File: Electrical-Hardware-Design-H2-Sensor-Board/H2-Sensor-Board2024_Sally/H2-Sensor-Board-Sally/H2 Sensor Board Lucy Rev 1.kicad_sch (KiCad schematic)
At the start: 55 parts, among them IC1 ESDALC6V1W5, J1 GPIO, J4 USB_B_Micro, J5 Conn_02x05_Top_Bottom, J8 OLED, Q2 NMOS IRLML2502TRPBF, SW1 SW_SPDT, SW2 RESET, U1 STM32L432KCU6, U10 8MHz, U10 MCP2542FD-E/SN, U7 FT234XD-R

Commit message: system update
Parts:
- added C1, C29, C30: 100n, Capacitor_SMD:C_0402_1005Metric, symbol Device:C
- added C10 (x2): 22u, Capacitor_SMD:CP_Elec_6.3x5.9, symbol Device:C_Polarized
- added C10: 100u, Capacitor_SMD:CP_Elec_6.3x5.9, symbol Device:C_Polarized
- added C15, C18: 100n, Capacitor_SMD:C_0603_1608Metric, symbol Device:C
- added C16, C17: 22u, Capacitor_SMD:C_1210_3225Metric, symbol Device:C
- added C2: 100n, Capacitor_SMD:C_0402_1005Metric, symbol Device:C_Small
- added C2: 100n, Capacitor_SMD:C_0603_1608Metric, symbol Device:C_Small
- added C21, C23: 10u, Capacitor_SMD:C_0805_2012Metric, symbol Device:C
- added C22, C24: 22u, Capacitor_SMD:C_0805_2012Metric, symbol Device:C
- added C25: 100n, Capacitor_SMD:C_0805_2012Metric, symbol Device:C
- added C28: 10u, Capacitor_SMD:C_1210_3225Metric, symbol Device:C
- added C32: 2n2, Capacitor_SMD:C_0402_1005Metric, symbol Device:C
- added C36, C37: 0u1, Capacitor_SMD:C_0603_1608Metric, symbol Device:C
- added C38: 4u7, Capacitor_SMD:C_0603_1608Metric, symbol Device:C
- added C39: 10n, Capacitor_SMD:C_0603_1608Metric, symbol Device:C
- added C40: 1u, Capacitor_SMD:C_0603_1608Metric, symbol Device:C
- added D1: GREEN, LED_SMD:LED_0805_2012Metric, symbol Device:LED
- added D11: BAT54C, Package_TO_SOT_SMD:SOT-23, symbol Diode:BAT54C
- added D14, D2, D3, D4: BLUE, LED_SMD:LED_0805_2012Metric, symbol Device:LED
- added D5: MMSZ5226B-7-F, Diode_SMD:D_SOD-123, symbol Device:D_Zener
- added D9: D_Schottky, Diode_SMD:D_0805_2012Metric, symbol Device:D_Schottky
- added F1: 500mA, Fuse:Fuse_0805_2012Metric, symbol Device:Polyfuse
- added FB2: 120R, Inductor_SMD:L_0603_1608Metric, symbol Device:FerriteBead_Small
- added J2: Conn_02x03_Top_Bottom, SYM&FOOT:Molex_Micro-Fit_3.0_43045-0621_2x03-1MP_P3.00mm_Horizontal, symbol Connector_Generic:Conn_02x03_Top_Bottom
- added JP1: Slave Address LSB 1, Jumper:SolderJumper-2_P1.3mm_Bridged_RoundedPad1.0x1.5mm, symbol Jumper:Jumper_2_Bridged
- added JP2: Slave Address LSB 0, Jumper:SolderJumper-2_P1.3mm_Open_RoundedPad1.0x1.5mm, symbol Jumper:Jumper_2_Open
- added JP3: MAX CURRENT, Jumper:SolderJumper-2_P1.3mm_Bridged_RoundedPad1.0x1.5mm, symbol Jumper:Jumper_2_Bridged
- added L1: 3u8, Inductor_SMD:L_12x12mm_H8mm, symbol Device:L
- added NT1: NetTie_2, NetTie:NetTie-2_SMD_Pad2.0mm, symbol Device:NetTie_2
- added Q1: NMOS, Package_TO_SOT_SMD:SOT-23, symbol Simulation_SPICE:NMOS
- added R1: 4k7, Resistor_SMD:R_0603_1608Metric, symbol Device:R_US
- added R10, R19: 560R, Resistor_SMD:R_0805_2012Metric, symbol Device:R
- added R11: 220R, Resistor_SMD:R_0805_2012Metric, symbol Device:R
- added R12, R7: 2k, Resistor_SMD:R_0805_2012Metric, symbol Device:R
- added R2: 620R, Resistor_SMD:R_0603_1608Metric, symbol Device:R
- added R20: R, Resistor_THT:R_Axial_DIN0204_L3.6mm_D1.6mm_P7.62mm_Horizontal, symbol Device:R
- added R21, R22, R3: 4k7, Resistor_SMD:R_0603_1608Metric, symbol Device:R
- added R27: 30k, Resistor_SMD:R_0603_1608Metric, symbol Device:R
- added R28: 47k, Resistor_SMD:R_0603_1608Metric, symbol Device:R
- added R30: 10k, Resistor_SMD:R_0805_2012Metric, symbol Device:R_US
- added R4, R8: 47k, Resistor_SMD:R_0805_2012Metric, symbol Device:R
- added R5: 23k7, Resistor_SMD:R_0805_2012Metric, symbol Device:R
- added R6: 511k, Resistor_SMD:R_0805_2012Metric, symbol Device:R
- added R9: 6k2, Resistor_SMD:R_0805_2012Metric, symbol Device:R
- added SW2: TARE, Button_Switch_THT:SW_PUSH_6mm_H5mm, symbol Switch:SW_Push
- added SW4: SW_SPDT, Button_Switch_SMD:SW_SPDT_PCM12, symbol Switch:SW_SPDT
- added TP3: MCO, TestPoint:TestPoint_Pad_D1.0mm, symbol Connector:TestPoint
- added U10: ~, SYM&FOOT:H2_Sensor_Daughter_Board_Rev_1, symbol H2_Parts:H2_Simon_Sensor_Breakout
- added U11: AD8603, Package_TO_SOT_SMD:TSOT-23-5, symbol Amplifier_Operational:AD8603
- added U12: STM32G474RET6, Package_QFP:LQFP-64_10x10mm_P0.5mm, symbol MCU_ST_STM32G4:STM32G474RETx
- added U3: AZ1117IH-5.0, Package_TO_SOT_SMD:SOT-223-3_TabPin2, symbol H2_Parts:AZ111IH-5.0
- added U4: TPS2596, Package_SO:TI_SO-PowerPAD-8, symbol H2_Parts:TPS2596
- added U5: AP62250, Package_TO_SOT_SMD:TSOT-23-6, symbol H2_Parts:AP62205
- added U6: AZ1117IH-3.3, Package_TO_SOT_SMD:SOT-223-3_TabPin2, symbol H2_Parts:AZ1117IH-3.3
- added U9: BME280, Package_LGA:Bosch_LGA-8_2.5x2.5mm_P0.65mm_ClockwisePinNumbering, symbol Sensor:BME280
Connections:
- net +3V3: now also C10.1, C24.1, C29.1, C30.1, C36.1, C37.1, C38.1, FB2.1, JP1.2 (B), R11.1, R21.1, R22.1, SW4.3 (C), U12.16 (VDD), U12.28 (VREF+), U12.32 (VDD), U12.48 (VDD), U12.64 (VDD), U6.2 (VO), U9.2 (CSB), U9.6 (VDDIO), U9.8 (VDD)
- net +5V: now also C10.1, C2.1, C22.1, C23.1, D11.1, R10.1, U11.5 (V+), U3.2 (VO), U6.3 (VI)
- net BOOT0: now also R30.2
- net CAN_RX: no longer U10.4 (RXD)
- net CAN_STBY: now also U12.42 (PA8); no longer U10.8 (STBY)
- net CAN_TX: no longer U10.1 (TXD)
- net GND: now also C1.1, C10.2, C10.2, C10.2, C15.2, C16.2, C17.2, C21.2, C22.2, C23.2, C24.2, C25.2, C28.2, C29.2, C30.2, C32.2, D14.1 (K), D2.1 (K), D3.1 (K), D4.1 (K), J2.2 (Pin_2), J2.5 (Pin_5), JP2.2 (B), JP3.2 (B), NT1.2, Q1.3 (S), R20.1, R27.1, R4.2, R9.1, SW2.1, SW4.1 (A), U12.1 (VBAT), U12.15 (VSS), U12.27 (VSSA), U12.31 (VSS), U12.47 (VSS), U12.63 (VSS), U3.1 (GND), U4.1 (GND), U4.9 (PAD), U5.1 (GND), U6.1 (GND), U9.1 (GND), U9.7 (GND)
- net GPLED1: now also U12.2 (PC13)
- net GPLED2: now also U12.3 (PC14)
- net GPLED3: now also U12.4 (PC15)
- net H2_SENSE: now also U12.40 (PC8)
- net NRST: now also U12.7 (PG10)
- net TARE: now also C1.2, SW2.2
- net UART_RX: now also U12.44 (PA10)
- net UART_TX: now also U12.43 (PA9)
- net VBUS_UP: now also D9.2 (A)
- net XCLK: now also U12.5 (PF0)
- new net: R27.2, R28.2, R3.2
- new net: C18.2, U5.6 (BST)
- new net: D3.2 (A), R11.2
- new net: D9.1 (K), F1.1
- new net: R4.1, R5.2, U4.8 (OVLO)
- new net: JP3.1 (A), R2.2, R20.2
- new net: R5.1, R6.1, U4.3 (EN/UVLO)
- new net: D11.3, U10.3 (V_HEAT)
- new net: D14.2 (A), R19.2
- new net: D1.2 (A), R7.2
- new net: D1.1 (K), Q1.1 (D)
- new net: C32.1, U4.2 (dV/dT)
- new net: D4.2 (A), R12.2
- new net: C39.1, C40.1, FB2.2, U12.29 (VDDA)
- new net: D2.2 (A), R10.2
- new net: R30.1, SW4.2 (B)
- new net: TP3.1, U12.55 (PD2)
- new net +12V: C10.1, C15.1, C28.1, U4.5 (OUT), U5.3 (VIN)
- new net 12V_UP: C25.1, J2.1 (Pin_1), J2.4 (Pin_4), R12.1, R28.1, R6.2, R7.1, U4.4 (IN)
- new net 5V_UP: J2.3 (Pin_3), J2.6 (Pin_6)
- new net 7V: C16.1, C17.1, C21.1, L1.2, R8.1, U3.3 (VI)
- new net ADDR: JP1.1 (A), JP2.1 (A), U9.5 (SDO)
- new net BOOT0?: U12.61 (PB8)
- new net FB: R8.2, R9.2, U5.4 (FB)
- new net FDCAN_RX: U10.4 (RXD), U12.45 (PA11)
- new net FDCAN_STBY: U10.8 (STBY)
- new net FDCAN_TX: U10.1 (TXD), U12.46 (PA12)
- new net GNDA: C2.2, C2.2, C36.2, C37.2, C38.2, C39.2, C40.2, D5.2 (A), NT1.1, R1.1, U10.1 (GND), U11.2 (V-)
- new net H2_ALARM: U12.37 (PB15)
- new net H2_CONC: D5.1 (K), U11.1, U11.4 (-)
- new net H2_SCL: U12.38 (PC6)
- new net H2_SDA: U12.39 (PC7)
- new net H2_TARE: U12.41 (PC9)
- new net I_{MON}: R2.1, U4.7 (ILM)
- new net SCL_BME: R22.2, U9.4 (SCK)
- new net SDA_BME: R21.2, U9.3 (SDI)
- new net SW: C18.1, L1.1, U5.2 (SW)
- new net SWCLK: U12.50 (PA14)
- new net SWDIO: U12.49 (PA13)
- new net V_HEAT: D11.2, F1.2, R19.1
- new net V_SENSE: C2.1, R1.2, U10.2 (V_SENSE), U11.3 (+)
- new net ~{FAULT}: Q1.2 (G), R3.1, U4.6 (~{FAULT})
- no-connect marks 11 -> 15
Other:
- added sheet signalling_edited (H2_Sensor_Board_Sally_R1.1.kicad_sch)
- note added: "1% tolerance"
- note added: "100n = u1"
- note added: "AP62250 Buck DC-DC Converter"
- note added: "BME280 Humidity, Temprature and Pressure sensor"
- note added: "C_{IN}"
- note added: "C_{IN} is increased just to be away from minimums"
- note added: "C_{IN}: As a rule of thumb, select an input capacitor with an RMS current rating greater than half of the maximum load current. I_{max} = 2.5;"
- note added: "C_{OUT}"
- note added: "C_{OUT}: Large capacitance and low ESR is the best option. 22µF to 68µF ceramic capacitor is sufficient. @NOTE: Size up Capacitors to next highest standard value. Maybe 47uF"
- note added: "Fault Indicator LED Turns Off when FAULT"
- note added: "From data sheet V_{OVLO} = 1.2V V_{UVLO} = 1.2V 1. V_{IN(ON)} = V_{OVLO(R} * (R1 + R2)/R2 2. V_{UVLO} = r2 + r3/ (r1 + r2 + r3) * V_{IN(UV)} 3. V_{OVLO} = r3 / (r1 + r2 + r3) * V_{IN(OV)} V_{OV} = 13V V_{UV} = 10V 1% r1 = 470k, r2 = 15, r3 = 47k V_{approx, OV} = 13.5V V_{approx, UV} = 10.3V rilm max = 464R; will give max 1.94A 845R will give 1A"
- note added: "I added a optional through hole resistor for limiting current."
- note added: "Inductor selection for AP63205"
- note added: "L = V_{OUT} * (V_{IN} - V_{OUT}) / (V_{IN} * Delta I_{L} * f_{SW}) Delta I_{L} = Inductor Ripple Current; 0.40 * 2A f_{SW} = buck switching frequency I_{L, PEAK} = I_{LOAD} + (Delta I_{L} / 2) I_{L, PEAK} determines the inductor saturation current. Saturating the inductor will decrease the efficency and increases the temprature. For most applications it is recommended inductance between 2.2 and 1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"
- note added: "MQ-8 Hydrogen Sensor Daughter Board"
- note added: "Phil's take: MAXIMUM SWITCHING CURRENT: Ensure IC can provide required current and use it to determine current rating for parts. 1. duty cycle partial = V_{Out} / (V_{In, max} * efficency) dcp = 5V / (12V * 0.85) = 0.49 2. Calculate Inductor Ripple Current: - use average L value from data sheet = (2.2 uH + 10 uH) / 2 = 6.1 uH Delta I_{L} = (12V - 5V) * 0.49 / (1100 * 10^3 * 6.1 * 10^-6 H) = 511 m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"
- note added: "Power Connection For PreHeater"
- note added: "STM32G474RET6"
- note added: "Standard 6 pin Molex for Power"
- note added: "TPS25963 eFuse 2A 12V"
- note added: "The data sheet for the AP63205 says the recommended component values are: L = 4.7 uH; C_{IN} = 10 uF; C_{OUT, 1 2} = 22 uH; C_{BST, SW} = 100 nF"
- note added: "r1 = 76k8 ; r2 = 10k; vout = 6.944V ish ¯\_(ツ)_/¯ L = 7*(12V - 7)/ (12V * 0.40 * 2.5A * 1300kHz * 10^3) = 3.846uH ~= 3.8uH I_{L peak} (Min Saturation Current) = I_{LOAD} + D I_{L}/2 = 2.5A + (0.4*2.5A)/2 = 3A Get I_{L peak} > 3.5A"
- note added: "things to add (33): - GPIO 1-8 - LED's (addressable)"
- note added: "things to add: - jumpers for testing 7v0, 5v0, 3v3"
- note added: "things to add: - life sensing LED"
- note added: "things to change: - DB7 male footprint change (check ecolib)"
- note added: "things to change: - STM32 JTAG connectors (FET board)"
- note added: "things to change: - TBD"
- note added: "things to change: - functionalize USB-C (check FET board)"
- note added: "use 5 mA for all LEDs"
- moved on the sheet: BZ1, C1, C10, C11, C12, C15, C16, C17, C54, C7, C8, C9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

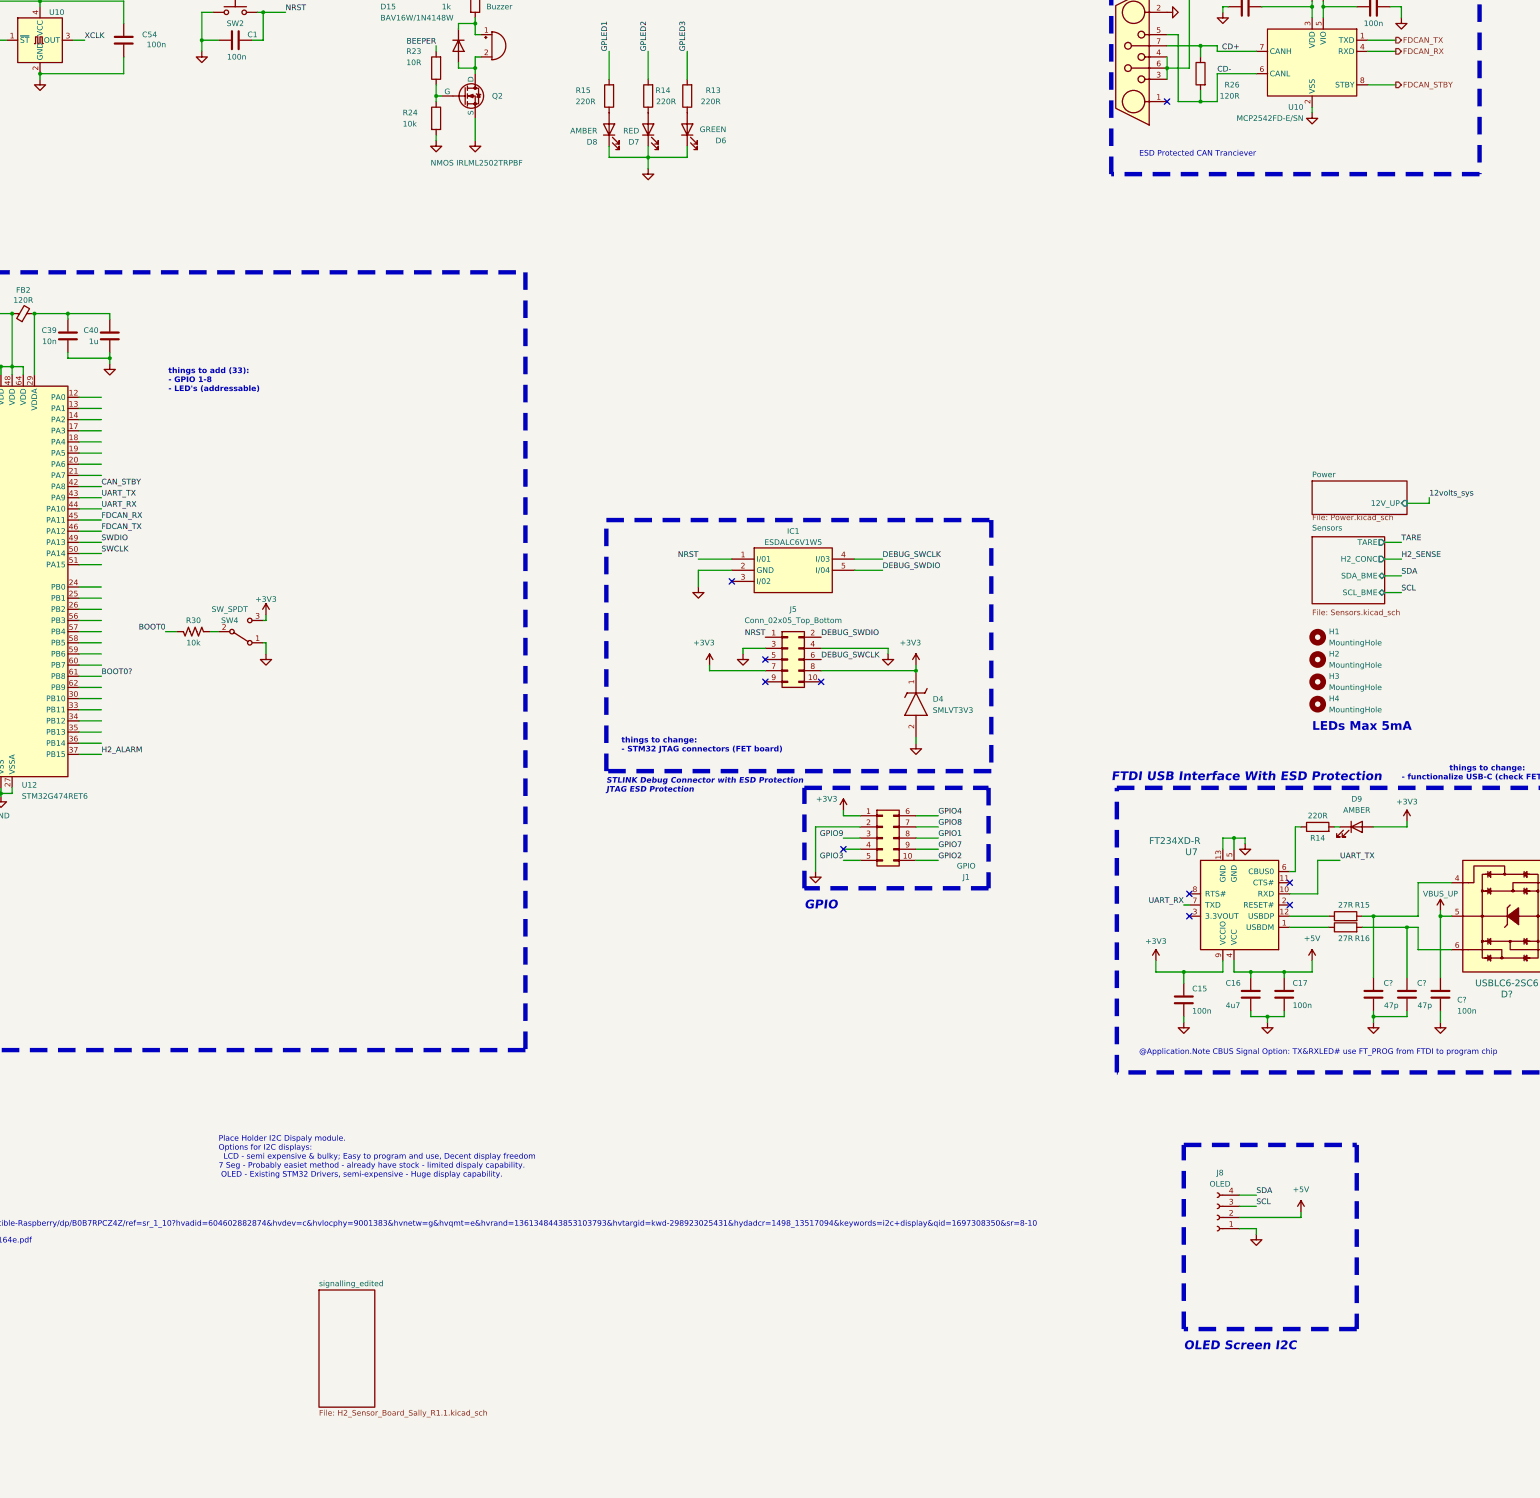
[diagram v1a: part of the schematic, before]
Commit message: add PC work to local machine
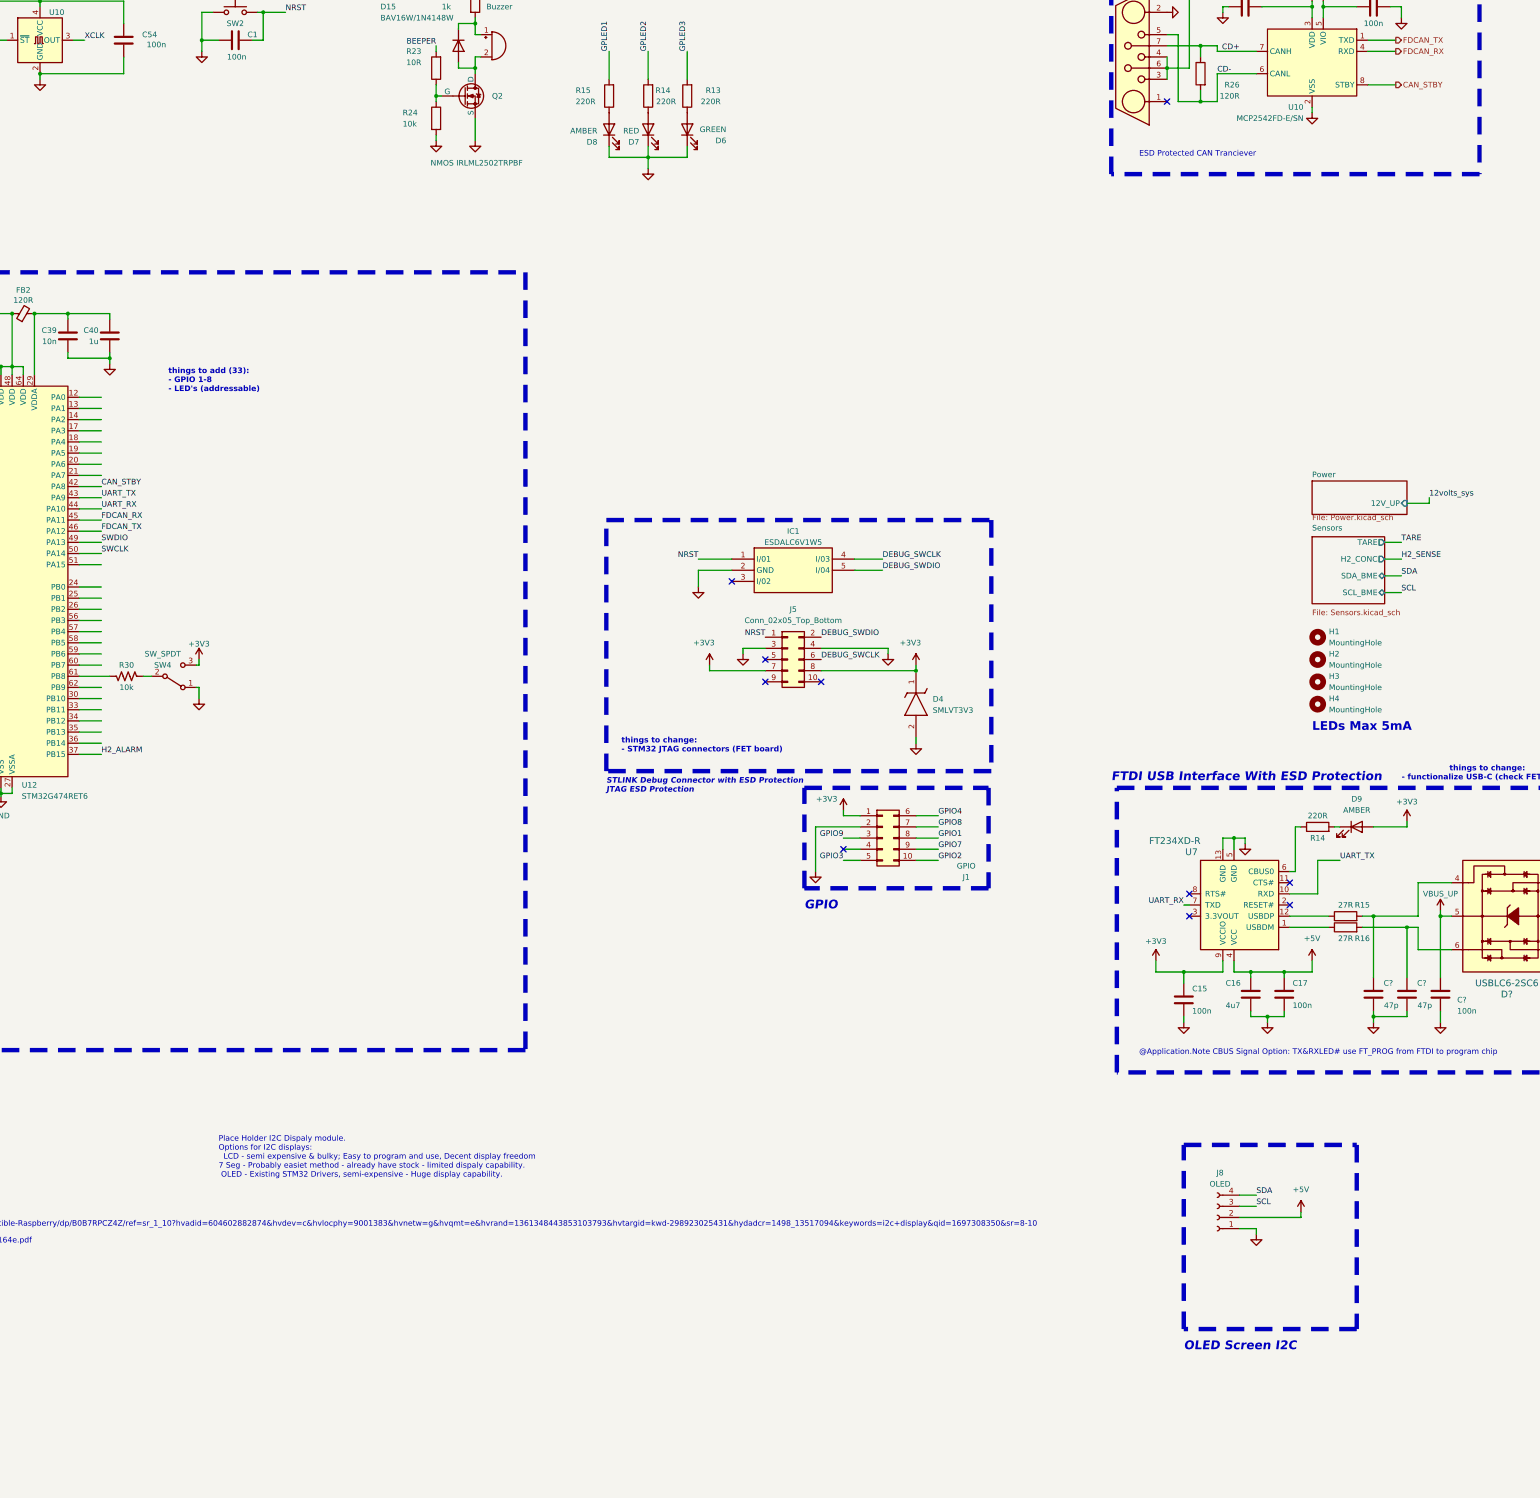
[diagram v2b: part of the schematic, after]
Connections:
- net FDCAN_STBY is gone; now on net CAN_STBY: U10.8 (STBY)
- net BOOT0: no longer R30.2
- net BOOT0?: no longer names the net of U12.61 (PB8)
- net BOOT0?: now also R30.2
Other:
- removed sheet signalling_edited
- moved on the sheet: R30, SW4
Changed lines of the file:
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@@
 	(wire
 		(pts
-			(xy 114.935 101.6) (xy 114.935 104.14)
+			(xy 99.695 111.76) (xy 99.695 114.3)
 		)
 		(stroke
@@
 	(wire
 		(pts
-			(xy 114.935 95.25) (xy 114.935 96.52)
+			(xy 99.695 105.41) (xy 99.695 106.68)
 		)
 		(stroke
@@
 	(wire
 		(pts
-			(xy 72.39 109.22) (xy 77.47 109.22)
+			(xy 72.39 109.22) (xy 79.375 109.22)
 		)
 		(stroke
@@
 	(wire
 		(pts
-			(xy 114.935 101.6) (xy 114.3 101.6)
+			(xy 99.695 111.76) (xy 99.06 111.76)
 		)
 		(stroke
@@
 	(wire
 		(pts
-			(xy 104.14 99.06) (xy 102.235 99.06)
+			(xy 88.9 109.22) (xy 86.995 109.22)
 		)
 		(stroke
@@
 	(wire
 		(pts
-			(xy 114.935 96.52) (xy 114.3 96.52)
+			(xy 99.695 106.68) (xy 99.06 106.68)
 		)
 		(stroke
@@
 	(wire
 		(pts
-			(xy 94.615 99.06) (xy 92.075 99.06)
-		)
-		(stroke
-			(width 0)
-			(type default)
-		)
-	)
-	(wire
-		(pts
 			(xy 77.47 60.96) (xy 72.39 60.96)
 		)
@@
 		)
 	)
-	(label "BOOT0"
-		(at 92.075 99.06 180)
-		(fields_autoplaced yes)
-		(effects
-			(font
-				(size 1.27 1.27)
-			)
-			(justify right bottom)
-		)
-	)
 	(label "SDA"
 		(at 373.38 86.36 0)
@@
 		)
 	)
-	(label "BOOT0?"
-		(at 77.47 109.22 0)
-		(fields_autoplaced yes)
-		(effects
-			(font
-				(size 1.27 1.27)
-			)
-			(justify left bottom)
-		)
-	)
 	(label "~{FAULT}"
 		(at -303.53 153.67 0)
@@
 		)
 	)
-	(hierarchical_label "FDCAN_STBY"
+	(hierarchical_label "CAN_STBY"
 		(shape output)
 		(at 372.11 -25.4 0)
@@
 	(symbol
 		(lib_id "power:GND")
-		(at 114.935 104.14 0)
+		(at 99.695 114.3 0)
 		(mirror y)
 		(unit 1)
@@
 		(dnp no)
 		(property "Reference" "#PWR086"
-			(at 114.935 110.49 0)
+			(at 99.695 120.65 0)
 			(effects
 				(font
@@
 		)
 		(property "Value" "GND"
-			(at 114.935 107.95 0)
+			(at 99.695 118.11 0)
 			(effects
 				(font
@@
 		)
 		(property "Footprint" ""
-			(at 114.935 104.14 0)
+			(at 99.695 114.3 0)
 			(effects
 				(font
@@
 		)
 		(property "Datasheet" ""
-			(at 114.935 104.14 0)
+			(at 99.695 114.3 0)
 			(effects
 				(font
@@
 		)
 		(property "Description" "Power symbol creates a global label with name \"GND\" , ground"
-			(at 114.935 104.14 0)
+			(at 99.695 114.3 0)
 			(effects
 				(font
@@
 	(symbol
 		(lib_id "power:+3V3")
-		(at 114.935 95.25 0)
+		(at 99.695 105.41 0)
 		(mirror y)
 		(unit 1)
@@
 		(dnp no)
 		(property "Reference" "#PWR049"
-			(at 114.935 99.06 0)
+			(at 99.695 109.22 0)
 			(effects
 				(font
@@
 		)
 		(property "Value" "+3V3"
-			(at 114.935 91.694 0)
+			(at 99.695 101.854 0)
 			(effects
 				(font
@@
 		)
 		(property "Footprint" ""
-			(at 114.935 95.25 0)
+			(at 99.695 105.41 0)
 			(effects
 				(font
@@
 		)
 		(property "Datasheet" ""
-			(at 114.935 95.25 0)
+			(at 99.695 105.41 0)
 			(effects
 				(font
@@
 		)
 		(property "Description" "Power symbol creates a global label with name \"+3V3\""
-			(at 114.935 95.25 0)
+			(at 99.695 105.41 0)
 			(effects
 				(font
@@
 	(symbol
 		(lib_id "Switch:SW_SPDT")
-		(at 109.22 99.06 0)
+		(at 93.98 109.22 0)
 		(mirror x)
 		(unit 1)
@@
 		(dnp no)
 		(property "Reference" "SW4"
-			(at 106.68 96.52 0)
+			(at 91.44 106.68 0)
 			(effects
 				(font
@@
 		)
 		(property "Value" "SW_SPDT"
-			(at 106.68 93.98 0)
+			(at 91.44 104.14 0)
 			(effects
 				(font
@@
 		)
 		(property "Footprint" "Button_Switch_SMD:SW_SPDT_PCM12"
-			(at 109.22 99.06 0)
+			(at 93.98 109.22 0)
 			(effects
 				(font
@@
 		)
 		(property "Datasheet" "~"
-			(at 109.22 99.06 0)
+			(at 93.98 109.22 0)
 			(effects
 				(font
@@
 		)
 		(property "Description" "Switch, single pole double throw"
-			(at 109.22 99.06 0)
+			(at 93.98 109.22 0)
 			(effects
 				(font
@@
 		)
 		(property "DK #" "2223-SLW-66527511-SMT-TRCT-ND"
-			(at 109.22 99.06 0)
+			(at 93.98 109.22 0)
 			(effects
 				(font
@@
 		)
 		(property "JLCPCB Part#(optional)" ""
-			(at 109.22 99.06 0)
+			(at 93.98 109.22 0)
 			(effects
 				(font
@@
 	(symbol
 		(lib_id "Device:R_US")
-		(at 98.425 99.06 270)
+		(at 83.185 109.22 270)
 		(mirror x)
 		(unit 1)
@@
 		(dnp no)
 		(property "Reference" "R30"
-			(at 98.425 96.52 90)
+			(at 83.185 106.68 90)
 			(effects
 				(font
@@
 		)
 		(property "Value" "10k"
-			(at 98.425 101.6 90)
+			(at 83.185 111.76 90)
 			(effects
 				(font
@@
 		)
 		(property "Footprint" "Resistor_SMD:R_0805_2012Metric"
-			(at 98.171 98.044 90)
+			(at 82.931 108.204 90)
 			(effects
 				(font
@@
 		)
 		(property "Datasheet" "~"
-			(at 98.425 99.06 0)
+			(at 83.185 109.22 0)
 			(effects
 				(font
@@
 		)
 		(property "Description" "Resistor, US symbol"
-			(at 98.425 99.06 0)
+			(at 83.185 109.22 0)
 			(effects
 				(font
@@
 		)
 		(property "JLCPCB Part#(Optional)" "C17414"
-			(at 98.425 99.06 0)
+			(at 83.185 109.22 0)
 			(effects
 				(font
@@
 		)
 		(property "JLCPCB Part#(optional)" "C17414"
-			(at 98.425 99.06 0)
+			(at 83.185 109.22 0)
 			(effects
 				(font
@@
 			)
 		)
-		(instances
-			(project "H2 Sensor Board Lucy Rev 1"
-				(path "/61fdd4a1-2d1e-44dc-8644-252e12d35745"
-					(page "4")
-				)
-			)
-		)
-	)
-	(sheet
-		(at 127 248.92)
-		(size 12.7 26.67)
-		(fields_autoplaced yes)
-		(stroke
-			(width 0.1524)
-			(type solid)
-		)
-		(fill
-			(color 0 0 0 0.0000)
-		)
-		(property "Sheetname" "signalling_edited"
-			(at 127 248.2084 0)
-			(effects
-				(font
-					(size 1.27 1.27)
-				)
-				(justify left bottom)
-			)
-		)
-		(property "Sheetfile" "H2_Sensor_Board_Sally_R1.1.kicad_sch"
-			(at 127 276.1746 0)
-			(effects
-				(font
-					(size 1.27 1.27)
-				)
-				(justify left top)
-			)
-		)
